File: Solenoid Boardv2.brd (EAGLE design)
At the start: 76.2 x 31.8 mm, 52 parts, among them Y2 ECS-80-S-4X

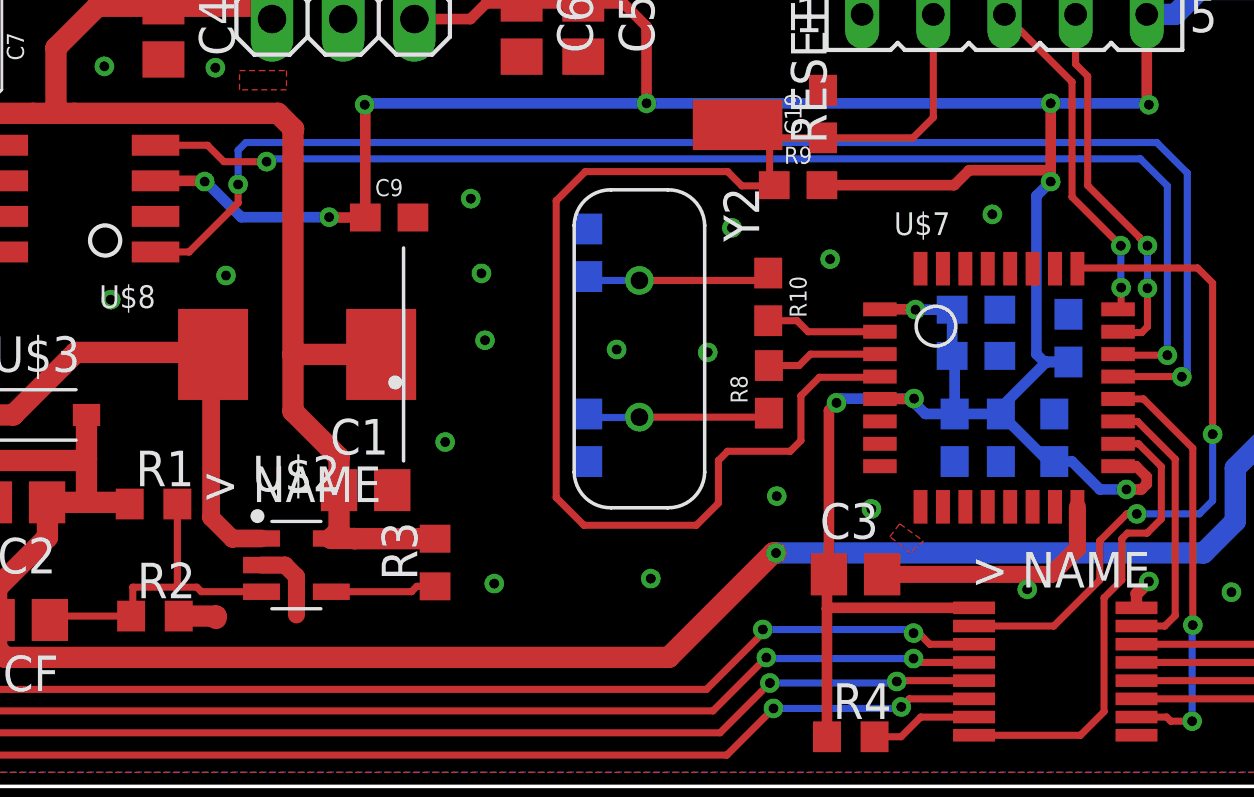
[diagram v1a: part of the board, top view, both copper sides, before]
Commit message: GND wasnt fully routed, fixed
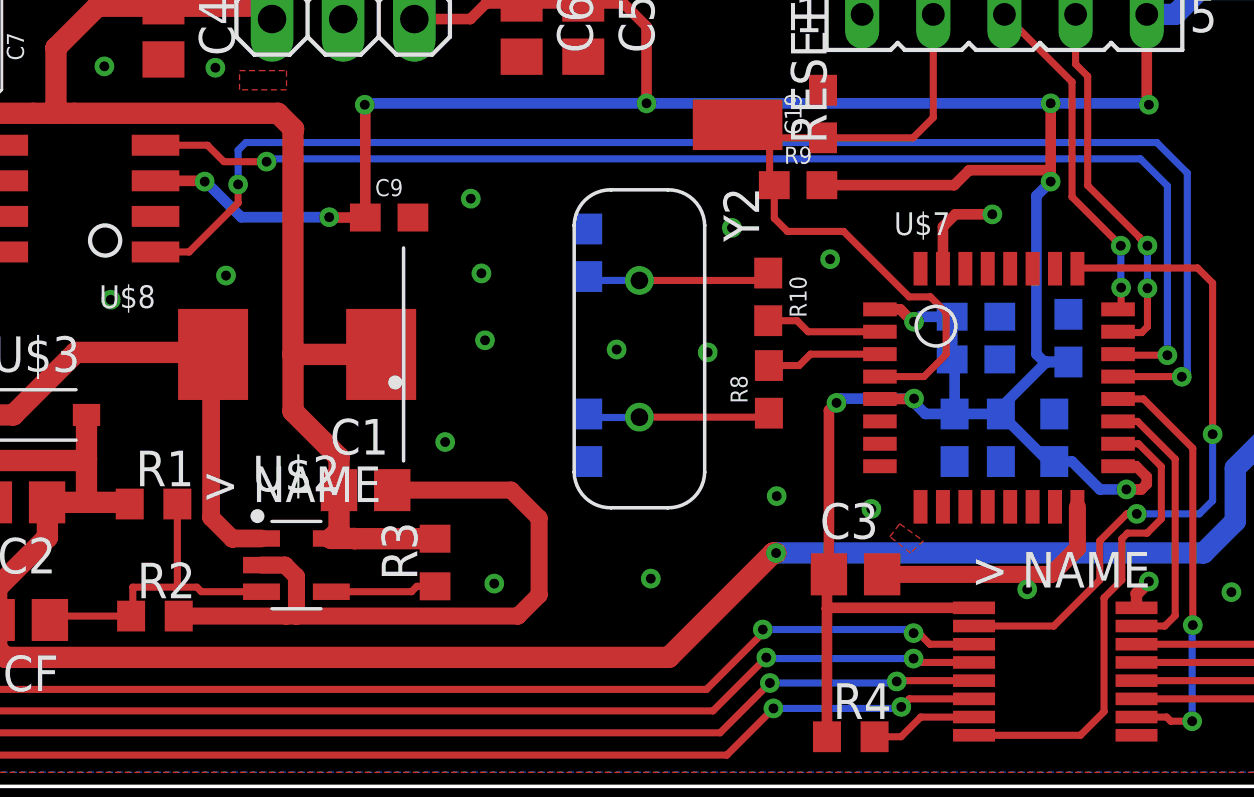
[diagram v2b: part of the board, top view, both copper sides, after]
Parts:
- moved C13 0.25 mm to (54.2, 16.8)
- moved C15 0.13 mm to (54.2, 15.2)
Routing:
- net GND: track 14.2 -> 37.8 mm
- net NRST: track 47.9 -> 25.8 mm
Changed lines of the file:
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@@
 <element name="U$5" library="BackplaneParts" package="T2I" value="T2I" x="6.35" y="6.35" rot="R90"/>
 <element name="U$6" library="board_outlines" package="PNE" value="BOARDPNE" x="0" y="0"/>
-<element name="C13" library="SparkFun-Capacitors" library_urn="urn:adsk.eagle:library:510" package="0603" package3d_urn="urn:adsk.eagle:package:37414/1" value="4.7uF" x="54.229" y="17.018" rot="MR180">
-<attribute name="NAME" x="54.229" y="16.256" size="0.6096" layer="26" font="vector" ratio="20" rot="MR180" align="bottom-center"/>
-<attribute name="PROD_ID" value="CAP-08280" x="54.229" y="17.018" size="1.778" layer="28" rot="MR180" display="off"/>
-<attribute name="VALUE" x="54.229" y="17.78" size="0.6096" layer="28" font="vector" ratio="20" rot="MR180" align="top-center"/>
+<element name="C13" library="SparkFun-Capacitors" library_urn="urn:adsk.eagle:library:510" package="0603" package3d_urn="urn:adsk.eagle:package:37414/1" value="4.7uF" x="54.229" y="16.764" rot="MR180">
+<attribute name="NAME" x="54.229" y="16.002" size="0.6096" layer="26" font="vector" ratio="20" rot="MR180" align="bottom-center"/>
+<attribute name="PROD_ID" value="CAP-08280" x="54.229" y="16.764" size="1.778" layer="28" rot="MR180" display="off"/>
+<attribute name="VALUE" x="54.229" y="17.526" size="0.6096" layer="28" font="vector" ratio="20" rot="MR180" align="top-center"/>
 </element>
 <element name="C14" library="SparkFun-Capacitors" library_urn="urn:adsk.eagle:library:510" package="0603" package3d_urn="urn:adsk.eagle:package:37414/1" value="4.7uF" x="57.023" y="12.446" rot="MR90">
@@
 <attribute name="VALUE" x="56.261" y="12.446" size="0.6096" layer="28" font="vector" ratio="20" rot="MR90" align="top-center"/>
 </element>
-<element name="C15" library="SparkFun-Capacitors" library_urn="urn:adsk.eagle:library:510" package="0603" package3d_urn="urn:adsk.eagle:package:37414/1" value="100nF" x="54.229" y="15.367" rot="MR180">
-<attribute name="NAME" x="54.229" y="14.605" size="0.6096" layer="26" font="vector" ratio="20" rot="MR180" align="bottom-center"/>
-<attribute name="PROD_ID" value="CAP-08280" x="54.229" y="15.367" size="1.778" layer="28" rot="MR180" display="off"/>
-<attribute name="VALUE" x="54.229" y="16.129" size="0.6096" layer="28" font="vector" ratio="20" rot="MR180" align="top-center"/>
+<element name="C15" library="SparkFun-Capacitors" library_urn="urn:adsk.eagle:library:510" package="0603" package3d_urn="urn:adsk.eagle:package:37414/1" value="100nF" x="54.229" y="15.24" rot="MR180">
+<attribute name="NAME" x="54.229" y="14.478" size="0.6096" layer="26" font="vector" ratio="20" rot="MR180" align="bottom-center"/>
+<attribute name="PROD_ID" value="CAP-08280" x="54.229" y="15.24" size="1.778" layer="28" rot="MR180" display="off"/>
+<attribute name="VALUE" x="54.229" y="16.002" size="0.6096" layer="28" font="vector" ratio="20" rot="MR180" align="top-center"/>
 </element>
 <element name="C16" library="SparkFun-Capacitors" library_urn="urn:adsk.eagle:library:510" package="0603" package3d_urn="urn:adsk.eagle:package:37414/1" value="100nF" x="57.531" y="16.002" rot="MR90">
@@
 <via x="15.8496" y="10.8712" extent="1-16" drill="0.35"/>
 <via x="17.0942" y="7.3914" extent="1-16" drill="0.35"/>
-<wire x1="25.77" y1="6.08" x2="27.1018" y2="6.08" width="0.762" layer="1"/>
-<wire x1="27.1018" y1="6.08" x2="27.1018" y2="5.9944" width="0.762" layer="1"/>
 <via x="23.114" y="25.7048" extent="1-16" drill="0.35"/>
 <via x="27.0764" y="25.654" extent="1-16" drill="0.35"/>
-<wire x1="28.7237" y1="7.9" x2="29.565" y2="7.9" width="0.6096" layer="1"/>
-<wire x1="29.972" y1="7.493" x2="29.972" y2="6.1214" width="0.6096" layer="1"/>
-<wire x1="29.565" y1="7.9" x2="29.972" y2="7.493" width="0.6096" layer="1"/>
 <polygon width="0.1524" layer="1">
 <vertex x="51.5112" y="9.3726"/>
@@
 </polygon>
 <wire x1="57.85" y1="9.98" x2="57.85" y2="8.4948" width="0.6096" layer="1"/>
-<wire x1="57.85" y1="8.4948" x2="57.8612" y2="8.4836" width="0.6096" layer="1"/>
 <via x="65.6082" y="16.4846" extent="1-16" drill="0.35"/>
 <via x="67.7418" y="11.9634" extent="1-16" drill="0.35"/>
@@
 <wire x1="59.96" y1="6.874" x2="60.4012" y2="7.3152" width="0.4572" layer="1"/>
 <wire x1="59.96" y1="6.375" x2="59.96" y2="6.874" width="0.4064" layer="1"/>
+<wire x1="53.05" y1="18.48" x2="53.05" y2="19.9792" width="0.381" layer="1"/>
+<wire x1="53.4924" y1="20.4216" x2="54.8132" y2="20.4216" width="0.381" layer="1"/>
+<wire x1="53.05" y1="19.9792" x2="53.4924" y2="20.4216" width="0.381" layer="1"/>
+<wire x1="28.7237" y1="7.9" x2="29.565" y2="7.9" width="0.6096" layer="1"/>
+<wire x1="29.565" y1="7.9" x2="29.972" y2="7.493" width="0.6096" layer="1"/>
+<wire x1="29.6004" y1="6.08" x2="25.77" y2="6.08" width="0.6096" layer="1"/>
+<wire x1="33.392" y1="10.5768" x2="37.6324" y2="10.5768" width="0.6096" layer="1"/>
+<wire x1="38.6334" y1="9.5758" x2="38.6334" y2="6.8326" width="0.6096" layer="1"/>
+<wire x1="38.6334" y1="6.8326" x2="37.8808" y2="6.08" width="0.6096" layer="1"/>
+<wire x1="37.8808" y1="6.08" x2="29.972" y2="6.08" width="0.6096" layer="1"/>
+<wire x1="29.972" y1="6.08" x2="29.6004" y2="6.08" width="0.6096" layer="1"/>
+<wire x1="37.6324" y1="10.5768" x2="38.6334" y2="9.5758" width="0.6096" layer="1"/>
+<wire x1="29.972" y1="7.493" x2="29.972" y2="6.08" width="0.6096" layer="1"/>
 </signal>
 <signal name="+12V">
@@
 <wire x1="47.029" y1="21.463" x2="46.863" y2="21.629" width="0.254" layer="1"/>
 <wire x1="46.863" y1="23.153" x2="46.863" y2="21.629" width="0.254" layer="1"/>
-<wire x1="50.775" y1="14.605" x2="48.641" y2="14.605" width="0.254" layer="1"/>
-<wire x1="50.8" y1="14.63" x2="50.775" y2="14.605" width="0.254" layer="1"/>
 <wire x1="48.768" y1="23.153" x2="51.982" y2="23.153" width="0.254" layer="1"/>
 <wire x1="52.705" y1="23.876" x2="52.705" y2="27.559" width="0.254" layer="1"/>
 <wire x1="52.705" y1="23.876" x2="51.982" y2="23.153" width="0.254" layer="1"/>
-<wire x1="48.641" y1="14.605" x2="47.9806" y2="13.9446" width="0.254" layer="1"/>
-<wire x1="47.9806" y1="13.9446" x2="47.9806" y2="12.3444" width="0.254" layer="1"/>
-<wire x1="47.9806" y1="12.3444" x2="47.5996" y2="11.9634" width="0.254" layer="1"/>
-<wire x1="47.5996" y1="11.9634" x2="45.3644" y2="11.9634" width="0.254" layer="1"/>
-<wire x1="45.3644" y1="11.9634" x2="45.0342" y2="11.6332" width="0.254" layer="1"/>
-<wire x1="45.0342" y1="10.1092" x2="44.2468" y2="9.3218" width="0.254" layer="1"/>
-<wire x1="44.2468" y1="9.3218" x2="40.2336" y2="9.3218" width="0.254" layer="1"/>
-<wire x1="40.2844" y1="21.9456" x2="39.243" y2="20.9042" width="0.254" layer="1"/>
-<wire x1="40.2844" y1="21.9456" x2="45.3644" y2="21.9456" width="0.254" layer="1"/>
-<wire x1="45.3644" y1="21.9456" x2="45.8724" y2="21.4376" width="0.254" layer="1"/>
-<wire x1="45.8724" y1="21.4376" x2="47.0036" y2="21.4376" width="0.254" layer="1"/>
-<wire x1="47.0036" y1="21.4376" x2="47.029" y2="21.463" width="0.254" layer="1"/>
-<wire x1="45.0342" y1="11.6332" x2="45.0342" y2="10.1092" width="0.254" layer="1"/>
-<wire x1="40.2336" y1="9.3218" x2="39.243" y2="10.3124" width="0.254" layer="1"/>
-<wire x1="39.243" y1="10.3124" x2="39.243" y2="20.9042" width="0.254" layer="1"/>
+<wire x1="47.029" y1="21.463" x2="47.029" y2="20.281" width="0.254" layer="1"/>
+<wire x1="47.029" y1="20.281" x2="47.498" y2="19.812" width="0.254" layer="1"/>
+<wire x1="47.498" y1="19.812" x2="49.5046" y2="19.812" width="0.254" layer="1"/>
+<wire x1="49.5046" y1="19.812" x2="51.8414" y2="17.4752" width="0.254" layer="1"/>
+<wire x1="50.8" y1="14.63" x2="52.3744" y2="14.63" width="0.254" layer="1"/>
+<wire x1="53.1622" y1="15.4178" x2="52.3744" y2="14.63" width="0.254" layer="1"/>
+<wire x1="51.8414" y1="17.4752" x2="52.6034" y2="17.4752" width="0.254" layer="1"/>
+<wire x1="53.1622" y1="16.9164" x2="53.1622" y2="15.4178" width="0.254" layer="1"/>
+<wire x1="52.6034" y1="17.4752" x2="53.1622" y2="16.9164" width="0.254" layer="1"/>
 </signal>
 <signal name="SWDIO">
@@
 <wire x1="57.658" y1="11.596" x2="58.654" y2="10.6" width="0.381" layer="16"/>
 <wire x1="58.654" y1="10.6" x2="59.6" y2="10.6" width="0.381" layer="16"/>
-<wire x1="53.467" y1="13.296" x2="53.467" y2="15.279" width="0.381" layer="16"/>
-<wire x1="53.467" y1="15.279" x2="53.379" y2="15.367" width="0.381" layer="16"/>
-<wire x1="53.379" y1="15.367" x2="53.379" y2="17.018" width="0.381" layer="16"/>
-<via x="52.07" y="17.018" extent="1-16" drill="0.35"/>
-<wire x1="52.07" y1="17.018" x2="52.058" y2="17.03" width="0.381" layer="1"/>
-<wire x1="52.058" y1="17.03" x2="50.8" y2="17.03" width="0.381" layer="1"/>
-<wire x1="53.379" y1="17.018" x2="52.07" y2="17.018" width="0.381" layer="16"/>
+<wire x1="53.467" y1="13.296" x2="53.467" y2="15.152" width="0.381" layer="16"/>
+<wire x1="53.467" y1="15.152" x2="53.379" y2="15.24" width="0.381" layer="16"/>
+<wire x1="53.379" y1="15.24" x2="53.379" y2="16.764" width="0.381" layer="16"/>
 <wire x1="56.6674" y1="15.152" x2="56.388" y2="15.4314" width="0.381" layer="16"/>
 <via x="56.896" y="21.59" extent="1-16" drill="0.35"/>
@@
 <wire x1="57.531" y1="15.152" x2="56.6674" y2="15.152" width="0.381" layer="16"/>
 <wire x1="55.118" y1="13.296" x2="55.118" y2="13.5246" width="0.381" layer="16"/>
+<wire x1="50.8" y1="17.03" x2="51.5246" y2="17.03" width="0.381" layer="1"/>
+<wire x1="51.9684" y1="16.5862" x2="52.0192" y2="16.5862" width="0.381" layer="1"/>
+<via x="52.0192" y="16.5862" extent="1-16" drill="0.35"/>
+<wire x1="52.0192" y1="16.5862" x2="52.197" y2="16.764" width="0.381" layer="16"/>
+<wire x1="52.197" y1="16.764" x2="53.379" y2="16.764" width="0.381" layer="16"/>
+<wire x1="51.5246" y1="17.03" x2="51.9684" y2="16.5862" width="0.381" layer="1"/>
 </signal>
 <signal name="N$4">

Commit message: Some changes that existed
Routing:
- net GND: vias 33 -> 37
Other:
- board text added: "Solenoid Board v1.0 Jan 2019 Callum Gundlach Jason King Grant Geyer"
